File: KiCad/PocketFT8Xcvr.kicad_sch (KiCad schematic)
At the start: 49 parts, among them J1 HX8357D, J2 ANT, J4 SI5351 BRK OUT, Q1 2N3904, Q2 2N3906, Q3 2N7000, Q4 2N7000, U1 MCP3422, U2 Si4735-D60-GU, U3 GVA-84

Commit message: Documentation update
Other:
- company: (none) -> KQ7B
- title: (none) -> Pocket FT8 Transceiver
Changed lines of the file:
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@@
 (kicad_sch (version 20230121) (generator eeschema)
   (paper "A4")
+  (title_block
+    (title "Pocket FT8 Transceiver")
+    (date "2024-07-31")
+    (rev "2.0")
+    (company "KQ7B")
+    (comment 1 "Original design by Charles Hill, Ricardo Caritti, Karlis Goba, Lars Petersen, et al")
+    (comment 2 "https://github.com/conr2286/PocketFT8Xcvr.git")
+  )
   (junction (at 207.01 119.38) (diameter 0) (color 0 0 0 0)
   )

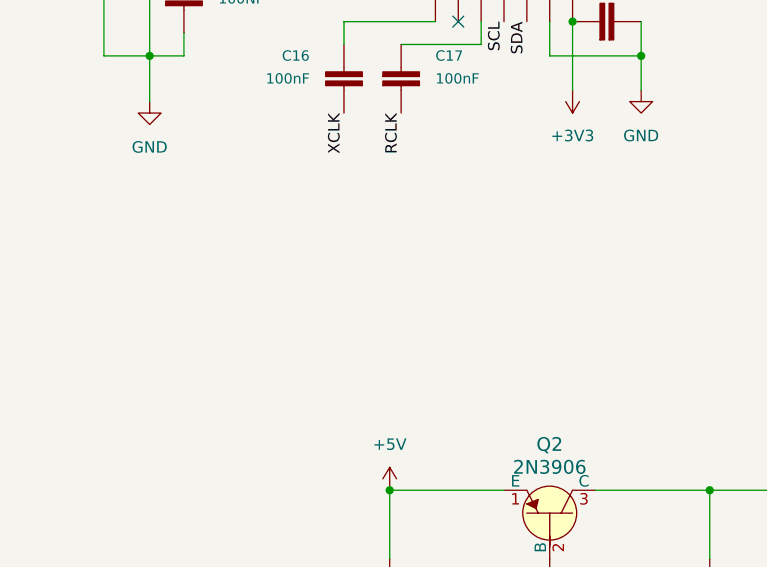
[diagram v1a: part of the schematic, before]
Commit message: Added the awful 7805 regulator
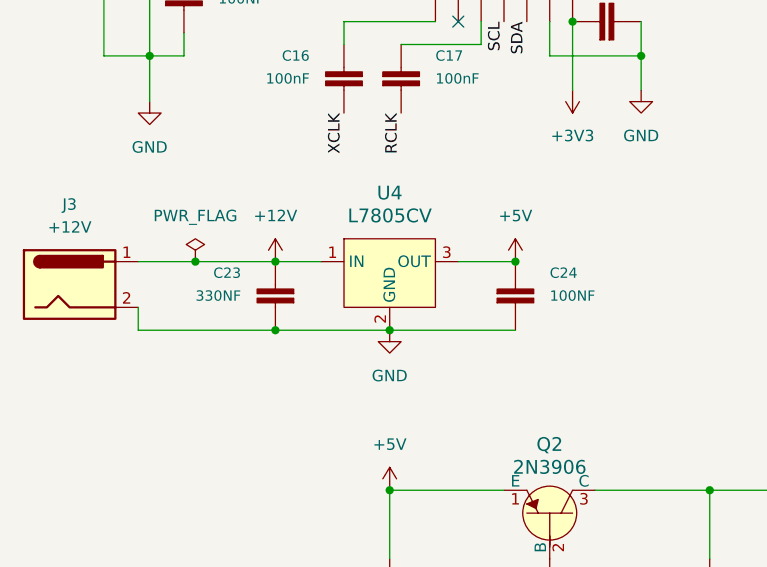
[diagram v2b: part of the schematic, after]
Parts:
- added C23: 330NF, 0603, symbol SparkFun-Capacitors:0.1UF-0603-25V-5%
- added C24: 100NF, 0603, symbol SparkFun-Capacitors:0.1UF-0603-25V-5%
- added J3: +12V, symbol Connector:Barrel_Jack
- added U4: L7805CV, digikey-footprints:TO-220-3, symbol dk_PMIC-Voltage-Regulators-Linear:L7805CV
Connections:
- net +5V: now also C24.1, U4.3 (OUT)
- net GND: now also C23.2, C24.2, J3.2, U4.2 (GND)
- new net +12V: C23.1, J3.1, U4.1 (IN)

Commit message: 1st Review of Schematic Capture
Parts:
- added C25: 100nF, 0603, symbol SparkFun-Capacitors:0.1UF-0603-25V-5%
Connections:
- net +3.3V: now also C18.2, J4.7 (VIN), C25.1
- net +3V3: no longer C18.2, J4.7 (VIN)
- net GND: now also C25.2
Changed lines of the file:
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@@
   (junction (at 207.01 119.38) (diameter 0) (color 0 0 0 0)
+  )
+  (junction (at 97.79 80.01) (diameter 0) (color 0 0 0 0)
   )
   (junction (at 279.4 119.38) (diameter 0) (color 0 0 0 0)
@@
     (stroke (width 0) (type default))
   )
+  (wire (pts (xy 97.79 80.01) (xy 104.14 80.01))
+    (stroke (width 0) (type default))
+  )
   (wire (pts (xy 219.71 20.32) (xy 232.41 20.32))
     (stroke (width 0) (type default))
@@
     (stroke (width 0) (type default))
   )
-  (wire (pts (xy 217.17 64.77) (xy 223.52 64.77))
+  (wire (pts (xy 215.9 64.77) (xy 223.52 64.77))
     (stroke (width 0) (type default))
   )
@@
     (stroke (width 0) (type default))
   )
+  (wire (pts (xy 165.1 39.37) (xy 165.1 44.45))
+    (stroke (width 0) (type default))
+  )
   (wire (pts (xy 52.07 57.15) (xy 72.39 57.15))
     (stroke (width 0) (type default))
@@
     (stroke (width 0) (type default))
   )
-  (wire (pts (xy 165.1 44.45) (xy 165.1 39.37))
-    (stroke (width 0) (type default))
-  )
   (wire (pts (xy 261.62 54.61) (xy 261.62 107.95))
     (stroke (width 0) (type default))
@@
     (stroke (width 0) (type default))
   )
-  (wire (pts (xy 217.17 62.23) (xy 223.52 62.23))
+  (wire (pts (xy 215.9 62.23) (xy 223.52 62.23))
     (stroke (width 0) (type default))
   )
@@
   )
   (wire (pts (xy 227.33 119.38) (xy 227.33 120.65))
+    (stroke (width 0) (type default))
+  )
+  (wire (pts (xy 90.17 80.01) (xy 97.79 80.01))
     (stroke (width 0) (type default))
   )
@@
     (effects (font (size 1.27 1.27)) (justify left bottom))
   )
-  (label "SCL" (at 217.17 62.23 0) (fields_autoplaced)
+  (label "SCL" (at 215.9 62.23 0) (fields_autoplaced)
     (effects (font (size 1.27 1.27)) (justify left bottom))
   )
@@
     (effects (font (size 1.27 1.27)) (justify left bottom))
   )
-  (label "SDA" (at 217.17 64.77 0) (fields_autoplaced)
+  (label "SDA" (at 215.9 64.77 0) (fields_autoplaced)
     (effects (font (size 1.27 1.27)) (justify left bottom))
   )
@@
   (label "X-" (at 160.02 92.71 0) (fields_autoplaced)
     (effects (font (size 1.27 1.27)) (justify left bottom))
+  )
+  (symbol (lib_id "SparkFun-Capacitors:0.1UF-0603-25V-5%") (at 97.79 85.09 0) (mirror y) (unit 1)
+    (in_bom yes) (on_board yes) (dnp no)
+    (property "Reference" "C25" (at 93.98 81.28 0)
+      (effects (font (size 1.143 1.143)) (justify left))
+    )
+    (property "Value" "100nF" (at 93.98 83.82 0)
+      (effects (font (size 1.143 1.143)) (justify left))
+    )
+    (property "Footprint" "0603" (at 97.79 78.74 0)
+      (effects (font (size 0.508 0.508)) hide)
+    )
+    (property "Datasheet" "" (at 97.79 85.09 0)
+      (effects (font (size 1.27 1.27)) hide)
+    )
+    (property "Field4" "" (at 93.98 86.36 0)
+      (effects (font (size 1.524 1.524)) (justify left) hide)
+    )
+    (pin "1")
+    (pin "2")
+    (instances
+      (project "PocketFT8Xcvr"
+        (path "/9b703ee0-e32d-4836-8d5c-bb1a7416ca3c"
+          (reference "C25") (unit 1)
+        )
+      )
+    )
   )
   (symbol (lib_id "power:+3.3V") (at 243.84 93.98 270) (unit 1)
@@
         (path "/9b703ee0-e32d-4836-8d5c-bb1a7416ca3c"
           (reference "#PWR07") (unit 1)
+        )
+      )
+    )
+  )
+  (symbol (lib_id "power:GND") (at 97.79 87.63 0) (unit 1)
+    (in_bom yes) (on_board yes) (dnp no) (fields_autoplaced)
+    (property "Reference" "#PWR027" (at 97.79 93.98 0)
+      (effects (font (size 1.27 1.27)) hide)
+    )
+    (property "Value" "GND" (at 97.79 92.71 0)
+      (effects (font (size 1.27 1.27)))
+    )
+    (property "Footprint" "" (at 97.79 87.63 0)
+      (effects (font (size 1.27 1.27)) hide)
+    )
+    (property "Datasheet" "" (at 97.79 87.63 0)
+      (effects (font (size 1.27 1.27)) hide)
+    )
+    (pin "1")
+    (instances
+      (project "PocketFT8Xcvr"
+        (path "/9b703ee0-e32d-4836-8d5c-bb1a7416ca3c"
+          (reference "#PWR027") (unit 1)
         )
       )
@@
     )
   )
+  (symbol (lib_id "power:+3.3V") (at 81.28 101.6 0) (mirror x) (unit 1)
+    (in_bom yes) (on_board yes) (dnp no)
+    (property "Reference" "#PWR036" (at 81.28 97.79 0)
+      (effects (font (size 1.27 1.27)) hide)
+    )
+    (property "Value" "+3.3V" (at 81.28 106.68 0)
+      (effects (font (size 1.27 1.27)))
+    )
+    (property "Footprint" "" (at 81.28 101.6 0)
+      (effects (font (size 1.27 1.27)) hide)
+    )
+    (property "Datasheet" "" (at 81.28 101.6 0)
+      (effects (font (size 1.27 1.27)) hide)
+    )
+    (pin "1")
+    (instances
+      (project "PocketFT8Xcvr"
+        (path "/9b703ee0-e32d-4836-8d5c-bb1a7416ca3c"
+          (reference "#PWR036") (unit 1)
+        )
+      )
+    )
+  )
   (symbol (lib_id "SparkFun-Resistors:2.0KOHM-0603-1_10W-5%") (at 78.74 158.75 270) (unit 1)
     (in_bom yes) (on_board yes) (dnp no)
@@
     )
   )
-  (symbol (lib_id "power:+3.3V") (at 104.14 80.01 90) (unit 1)
-    (in_bom yes) (on_board yes) (dnp no) (fields_autoplaced)
-    (property "Reference" "#PWR05" (at 107.95 80.01 0)
-      (effects (font (size 1.27 1.27)) hide)
-    )
-    (property "Value" "+3.3V" (at 100.33 80.01 90)
+  (symbol (lib_id "power:+3.3V") (at 90.17 80.01 90) (unit 1)
+    (in_bom yes) (on_board yes) (dnp no) (fields_autoplaced)
+    (property "Reference" "#PWR05" (at 93.98 80.01 0)
+      (effects (font (size 1.27 1.27)) hide)
+    )
+    (property "Value" "+3.3V" (at 86.36 80.01 90)
       (effects (font (size 1.27 1.27)) (justify left))
     )
-    (property "Footprint" "" (at 104.14 80.01 0)
-      (effects (font (size 1.27 1.27)) hide)
-    )
-    (property "Datasheet" "" (at 104.14 80.01 0)
+    (property "Footprint" "" (at 90.17 80.01 0)
+      (effects (font (size 1.27 1.27)) hide)
+    )
+    (property "Datasheet" "" (at 90.17 80.01 0)
       (effects (font (size 1.27 1.27)) hide)
     )
@@
         )
       )
-    )
-  )
-  (symbol (lib_id "power:+3V3") (at 81.28 101.6 0) (mirror x) (unit 1)
-    (in_bom yes) (on_board yes) (dnp no)
-    (property "Reference" "#PWR027" (at 81.28 97.79 0)
-      (effects (font (size 1.27 1.27)) hide)
-    )
-    (property "Value" "+3V3" (at 81.28 106.68 0)
-      (effects (font (size 1.27 1.27)))
-    )
-    (property "Footprint" "" (at 81.28 101.6 0)
-      (effects (font (size 1.27 1.27)) hide)
-    )
-    (property "Datasheet" "" (at 81.28 101.6 0)
-      (effects (font (size 1.27 1.27)) hide)
-    )
-    (pin "1")
-    (instances
-      (project "PocketFT8Xcvr"
-        (path "/9b703ee0-e32d-4836-8d5c-bb1a7416ca3c"
-          (reference "#PWR027") (unit 1)
-        )
-      )

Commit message: Results from LP Filter Simulation
2nd harmonic rejection of the original low pass filter is greatly improved with inclusion of a 36 mHz trap.  The current version of the truth is to include the trap capacitor paralled with L1 (value unchanged) in the schematic, but don't load the board with the trap components until after spectral testing confims it's necessary.
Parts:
- added C26: (no value), symbol SparkFun-Capacitors:47PF-0603-50V-5%
- L1, L2: value L_Ferrite -> 0.5uH
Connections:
- net at C8.1, J2.2, L1.2: now also C26.2
- net at C9.1, L1.1, L2.2: now also C26.1
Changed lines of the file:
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@@
+    (stroke (width 0) (type default))
+  )
+  (wire (pts (xy 259.08 132.08) (xy 264.16 132.08))
     (stroke (width 0) (type default))
   )
@@
     (stroke (width 0) (type default))
   )
+  (wire (pts (xy 264.16 132.08) (xy 264.16 142.24))
+    (stroke (width 0) (type default))
+  )
   (wire (pts (xy 39.37 120.65) (xy 48.26 120.65))
     (stroke (width 0) (type default))
@@
     (stroke (width 0) (type default))
   )
+  (wire (pts (xy 245.11 132.08) (xy 251.46 132.08))
+    (stroke (width 0) (type default))
+  )
   (wire (pts (xy 241.3 39.37) (xy 236.22 39.37))
     (stroke (width 0) (type default))
@@
   )
   (wire (pts (xy 96.52 186.69) (xy 96.52 171.45))
+    (stroke (width 0) (type default))
+  )
+  (wire (pts (xy 245.11 142.24) (xy 245.11 132.08))
     (stroke (width 0) (type default))
   )
@@
         (path "/9b703ee0-e32d-4836-8d5c-bb1a7416ca3c"
           (reference "#FLG01") (unit 1)
+        )
+      )
+    )
+  )
+  (symbol (lib_id "SparkFun-Capacitors:47PF-0603-50V-5%") (at 256.54 132.08 90) (unit 1)
+    (in_bom yes) (on_board yes) (dnp no)
+    (property "Reference" "C26" (at 255.27 128.27 90)
+      (effects (font (size 1.143 1.143)))
+    )
+    (property "Value" "" (at 255.27 128.27 90)
+      (effects (font (size 1.143 1.143)))
+    )
+    (property "Footprint" "" (at 250.19 132.08 0)
+      (effects (font (size 0.508 0.508)) hide)
+    )
+    (property "Datasheet" "" (at 256.54 132.08 0)
+      (effects (font (size 1.27 1.27)) hide)
+    )
+    (property "Field4" "" (at 255.27 128.27 90)
+      (effects (font (size 1.524 1.524)) hide)
+    )
+    (pin "2")
+    (pin "1")
+    (instances
+      (project "PocketFT8Xcvr"
+        (path "/9b703ee0-e32d-4836-8d5c-bb1a7416ca3c"
+          (reference "C26") (unit 1)
         )
       )
@@
       (effects (font (size 1.27 1.27)))
     )
-    (property "Value" "L_Ferrite" (at 255.27 138.43 90)
+    (property "Value" "0.5uH" (at 255.27 138.43 90)
       (effects (font (size 1.27 1.27)))
     )
@@
       (effects (font (size 1.27 1.27)))
     )
-    (property "Value" "L_Ferrite" (at 236.22 138.43 90)
+    (property "Value" "0.5uH" (at 236.22 138.43 90)
       (effects (font (size 1.27 1.27)))
     )
